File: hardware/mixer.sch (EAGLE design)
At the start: 169 parts, among them IC1 PGA2311, IC11 OPA2134P, IC12 OPA2134P, IC2 PGA2311, IC3 PGA2311, IC4 PGA2311, IC5 PGA2311, IC6 OPA2134P, IC7 OPA2134P, IC8 OPA2134P, IC9 OPA2134P, Q1 SI2305, Q2 MOSFET-NCHANNEL_SOT23-3, X1 MOLEX_6HORIZONTAL, X2 MOLEX_6VERTICAL, X3 MOLEX_4VERTICAL, Y1 32768Hz CFPX-217 12.5pF

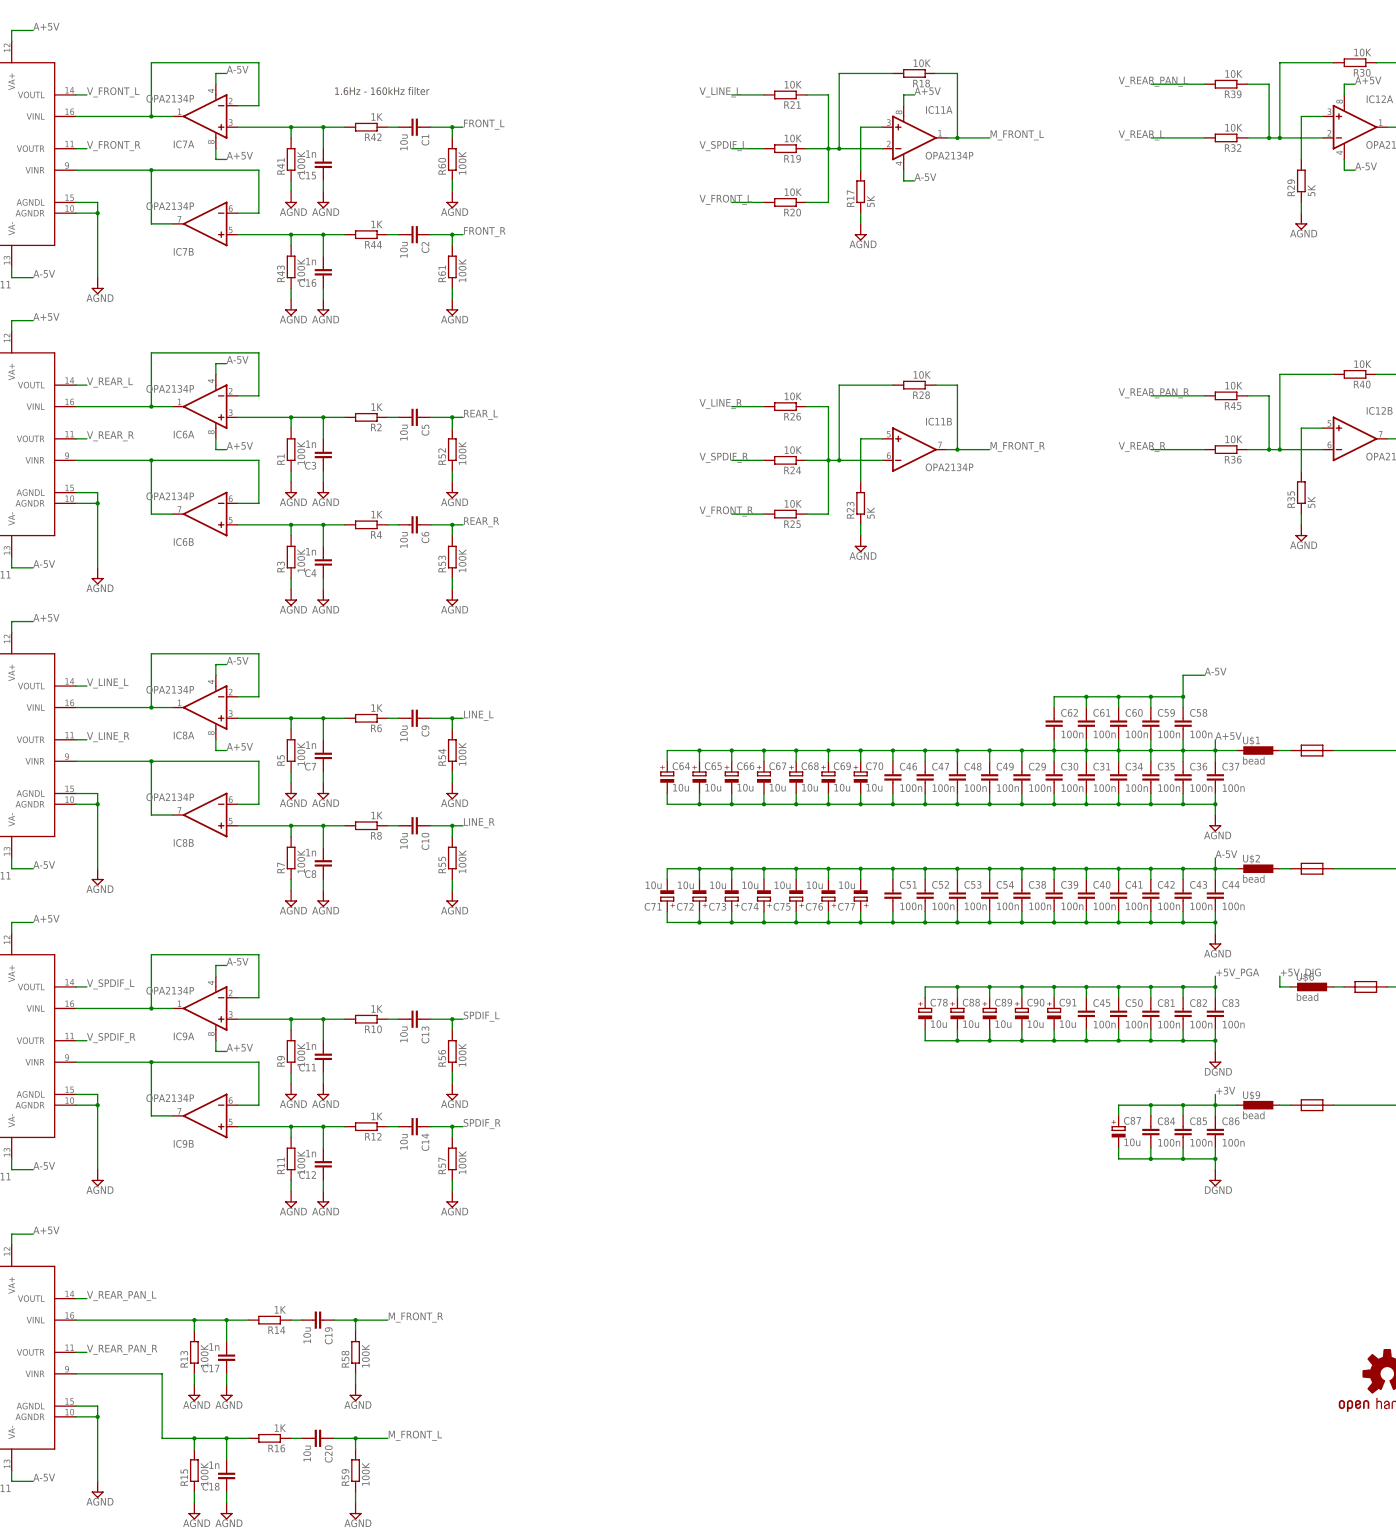
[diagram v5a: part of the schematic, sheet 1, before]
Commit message: add jumper for pan input
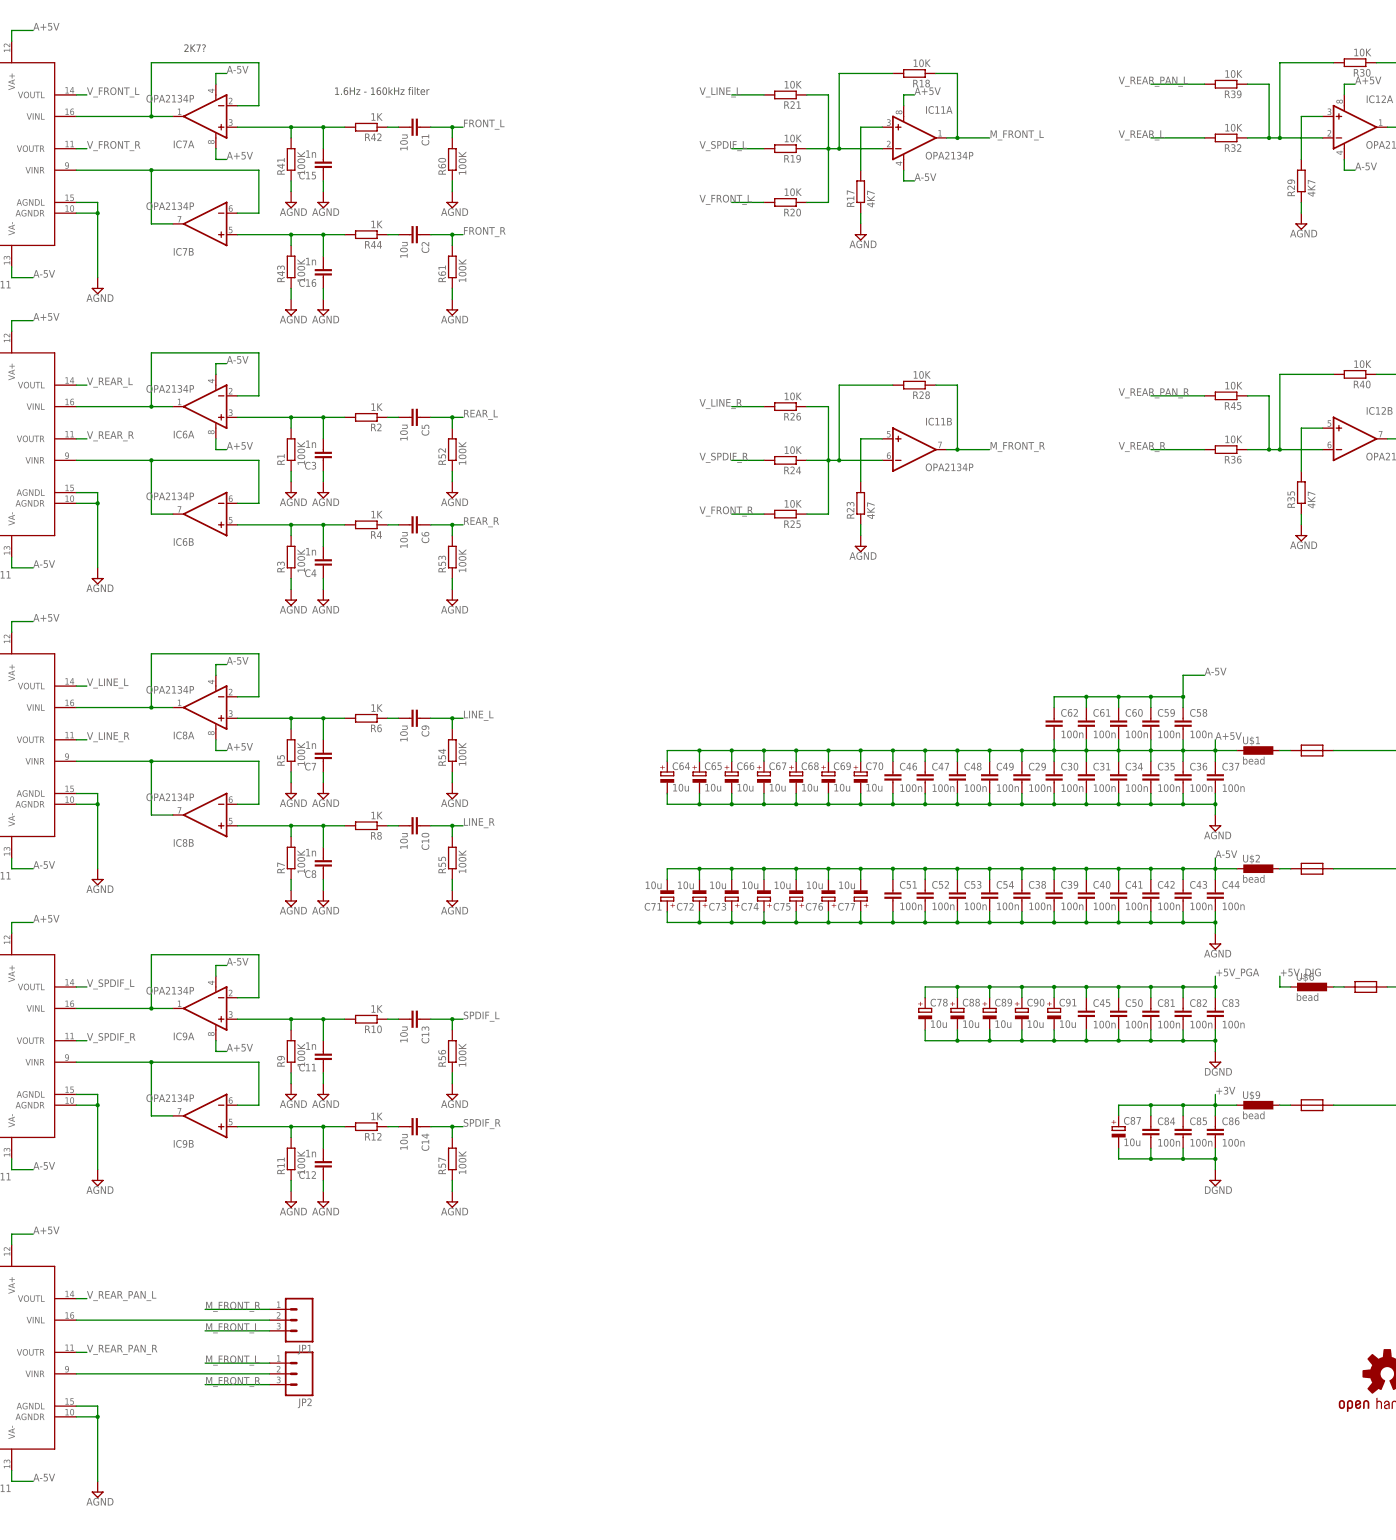
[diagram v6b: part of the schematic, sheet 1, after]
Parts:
- removed C17, C18: 1n, rcl:C-EUC0805
- removed C19, C20: 10u, rcl:C-EUC0805
- removed R13, R15, R58, R59: 100K, rcl:R-EU_R0805W
- removed R14, R16: 1K, rcl:R-EU_R0805W
- added JP1, JP2: (no value), SparkFun-Connectors:M03PTH
- R17, R23, R29, R35: value 5K -> 4K7
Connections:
- removed net N$37: C18.2, IC5.VINR, R15.2, R16.2
- removed net N$43: C20.2, R16.1
- net AGND: no longer C17.1, C18.1, R13.1, R15.1, R58.1, R59.1
- net M_FRONT_L: now also JP1.3, JP2.1; no longer C20.1, R59.2
- net M_FRONT_R: now also JP1.1, JP2.3; no longer C19.1, R58.2
- net N$36: now also JP1.2; no longer C17.2, R13.2, R14.2
- net N$42: now also IC5.VINR, JP2.2; no longer C19.2, R14.1
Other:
- note added: "2K7?"

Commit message: change input filters - agin
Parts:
- added R13, R14: 100K, rcl:R-EU_R0805W
- added R15, R16, R58, R59, R62, R63: DNP, rcl:R-EU_R0805W
- C1, C10, C13, C14, C2, C5, C6, C9: value 10u -> 1u
- R41, R43, R52, R53, R54, R55, R56, R57, R60, R61: value 100K -> DNP
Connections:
- net AGND: now also R13.1, R14.1, R15.1, R16.1, R58.1, R59.1, R62.1, R63.1
- net N$1: now also R1.2
- net N$11: now also R5.2
- net N$12: now also R7.2
- net N$18: now also R59.2; no longer R7.2
- net N$2: now also R3.2
- net N$20: now also R58.2; no longer R5.2
- net N$22: now also R9.2
- net N$23: now also R11.2
- net N$27: now also R63.2; no longer R11.2
- net N$28: now also R62.2; no longer R9.2
- net N$29: now also R16.2; no longer R43.2
- net N$31: now also R13.2
- net N$32: now also R14.2
- net N$33: now also R15.2; no longer R41.2
- net N$8: now also R43.2; no longer R3.2
- net N$9: now also R41.2; no longer R1.2
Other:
- moved on the sheet: C1, C10, C13, C14, C2, C5, C6, C9, R1, R11, R3, R41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

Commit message: started routing
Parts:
- removed U$1, U$2, U$6, U$9: bead, Simplex-rlc:INDUCTOR
- added IC10, IC13: OPA2134P, burr-brown:OPA2134P
- added R64, R65, R78, R80, R81, R82, R83, R84, R88, R91, R92, R93, R94, R95: 0R_0805, Simplex-Jumpers:0R_0805
- added R66, R79: 0R, rcl:R-EU_R0805W
- added R67, R70, R73, R76: 4K7, rcl:R-EU_R0805W
- added R68, R69, R71, R72, R74, R77, R86, R89: 10K, rcl:R-EU_R0805W
- added R75, R85, R87, R90: DNP, rcl:R-EU_R0805W
- JP1: value (none) -> J1
- JP2: value (none) -> J2
- X2: value MOLEX_6VERTICAL -> MOLEX_6HORIZONTAL; device Simplex-Connectors:MOLEX_6VERTICAL -> Simplex-Connectors:MOLEX_6HORIZONTAL
- X3: value MOLEX_4VERTICAL -> MOLEX_4HORIZONTAL; device Simplex-Connectors:MOLEX_4VERTICAL -> Simplex-Connectors:MOLEX_4HORIZONTAL
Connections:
- new net N$37: IC6A.-IN, R64.P$2
- new net N$43: IC6B.-IN, R65.P$2
- new net N$48: IC7A.-IN, R66.1
- new net N$49: IC10A.OUT, R18.1, R84.P$2
- new net N$50: IC7B.-IN, R79.1
- new net N$54: IC10B.+IN, R67.2
- new net N$55: IC10B.-IN, R68.2, R69.1
- new net N$56: IC8A.-IN, R80.P$2
- new net N$61: IC11B.+IN, R70.2
- new net N$66: IC11B.-IN, R71.2, R72.1
- new net N$67: IC8B.-IN, R81.P$2
- new net N$68: IC12B.+IN, R73.2
- new net N$69: IC12B.-IN, R74.2, R86.1
- new net N$70: IC9A.-IN, R82.P$2
- new net N$71: IC13B.+IN, R76.2
- new net N$72: IC13B.-IN, R77.2, R89.1
- new net N$73: IC9B.-IN, R83.P$2
- new net N$75: IC11A.OUT, R28.1, R78.P$2
- new net N$76: IC12A.OUT, R30.1, R88.P$2
- new net N$77: R69.2, R84.P$1, R85.1
- new net N$78: IC13A.OUT, R40.1, R91.P$2
- new net N$81: R72.2, R75.1, R78.P$1
- new net N$84: R86.2, R87.1, R88.P$1
- new net N$87: R89.2, R90.1, R91.P$1
- net +3V: now also R95.P$2; no longer U$9.2
- net +5V_DIG: now also R92.P$1; no longer U$6.2
- net A+5V: now also IC10A.V+, IC13A.V+, R94.P$1; no longer U$1.2
- net A-5V: now also IC10A.V-, IC13A.V-, R93.P$1; no longer U$2.2
- net AGND: now also R67.1, R70.1, R73.1, R75.2, R76.1, R85.2, R87.2, R90.2, X2.6; no longer X2.1
- net DGND: now also U$11.39, U$11.41, X2.1; no longer X2.6
- net M_FRONT_L: now also IC10B.OUT, R68.1; no longer IC11A.OUT, R18.1
- net M_FRONT_R: now also R71.1; no longer R28.1
- net M_REAR_L: now also IC12B.OUT, R74.1; no longer IC12A.OUT, R30.1
- net M_REAR_R: now also IC13B.OUT, R77.1; no longer IC12B.OUT, R40.1
- net N$15: now also R80.P$1; no longer IC8A.-IN
- net N$16: now also R81.P$1; no longer IC8B.-IN
- net N$17: now also IC6B.OUT, R65.P$1; no longer IC7B.-IN, IC7B.OUT
- net N$19: now also R82.P$1; no longer IC9A.-IN
- net N$24: now also X2.4; no longer X2.3
- net N$25: now also X2.3; no longer X2.4
- net N$26: now also R83.P$1; no longer IC9B.-IN
- net N$29: now also IC6B.+IN; no longer IC7B.+IN
- net N$3: now also R92.P$2; no longer U$6.1
- net N$33: now also IC6A.+IN; no longer IC7A.+IN
- net N$34: now also X2.2; no longer X2.5
- net N$4: now also IC7A.OUT, R66.2; no longer IC6A.-IN, IC6A.OUT
- net N$46: now also IC10A.+IN; no longer IC11A.+IN
- net N$47: now also IC10A.-IN; no longer IC11A.-IN
- net N$5: now also IC6A.OUT, R64.P$1; no longer IC7A.-IN, IC7A.OUT
- net N$51: now also IC13A.-IN; no longer IC12B.-IN
- net N$52: now also IC11A.+IN; no longer IC11B.+IN
- net N$53: now also IC11A.-IN; no longer IC11B.-IN
- net N$6: now also R95.P$1; no longer U$9.1
- net N$60: now also R94.P$2; no longer U$1.1
- net N$62: now also R93.P$2; no longer U$2.1
- net N$63: now also X2.5; no longer X2.2
- net N$64: now also IC13A.+IN; no longer IC12B.+IN
- net N$7: now also IC7B.OUT, R79.2; no longer IC6B.-IN, IC6B.OUT
- net N$8: now also IC7B.+IN; no longer IC6B.+IN
- net N$9: now also IC7A.+IN; no longer IC6A.+IN
- net V_FRONT_L: now also R19.2; no longer R20.2
- net V_FRONT_R: now also R24.2; no longer R25.2
- net V_LINE_L: now also R20.2; no longer R21.2
- net V_LINE_R: now also R25.2; no longer R26.2
- net V_REAR_L: now also R39.2; no longer R32.2
- net V_REAR_PAN_L: now also R32.2; no longer R39.2
- net V_REAR_PAN_R: now also R36.2; no longer R45.2
- net V_REAR_R: now also R45.2; no longer R36.2
- net V_SPDIF_L: now also R21.2; no longer R19.2
- net V_SPDIF_R: now also R26.2; no longer R24.2
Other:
- note added: "o"
- note removed: "2K7?"
- moved on the sheet: C10, C11, C12, C13, C14, C29, C3, C30, C31, C34, C35, C36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
